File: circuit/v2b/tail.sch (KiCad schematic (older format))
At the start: 47 parts, among them J1 LED_DEBUG, J11 UART, J19 LiPo, J2 POWER_DEBUG, J25 USB_OTG, J3 LiPo, J9 DEBUG, Q1 Q_NMOS_GSD, SW1 SW_SPDT, U1 DWM1000, U2 EFM32HG222F64, U3 MC3630, U4 XC6215B332NR, U5 MCP73831-2-OT, Y1 32.768kHz CFPX-217 20ppm 7pF

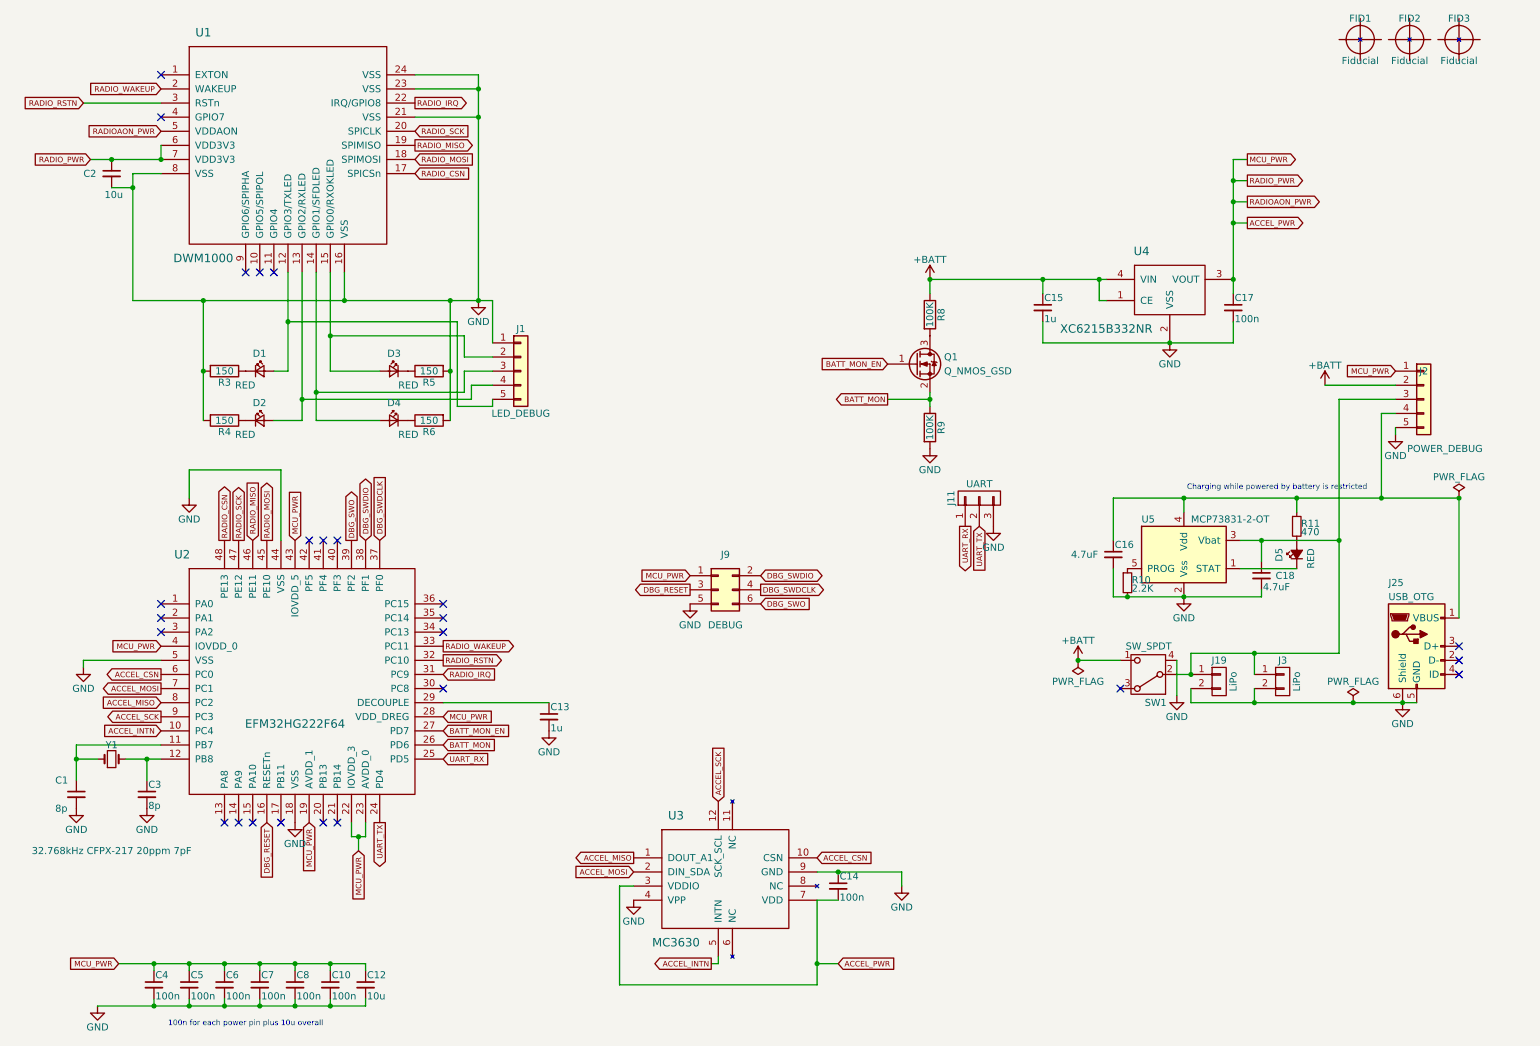
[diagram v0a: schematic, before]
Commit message: circuit: Add UART-USB level shifting and reduce charge current
We need to connect the UART to the USB data pins. As these will present
5 volts, we need to add level shifting to protect the 3.3 volt mcu.

We will need to enable the internal pullup on the UART Rx line.
The host cable we are proposing to use already has a pullup on its
Rx line.

While we're here, reduce the charge current to just under 200mA in
order to meet the 0.5C charge current specification on the 400mAh
batteries that we're using.

Signed-off-by: Gavan Fantom <gavan.fantom@unipart.io>
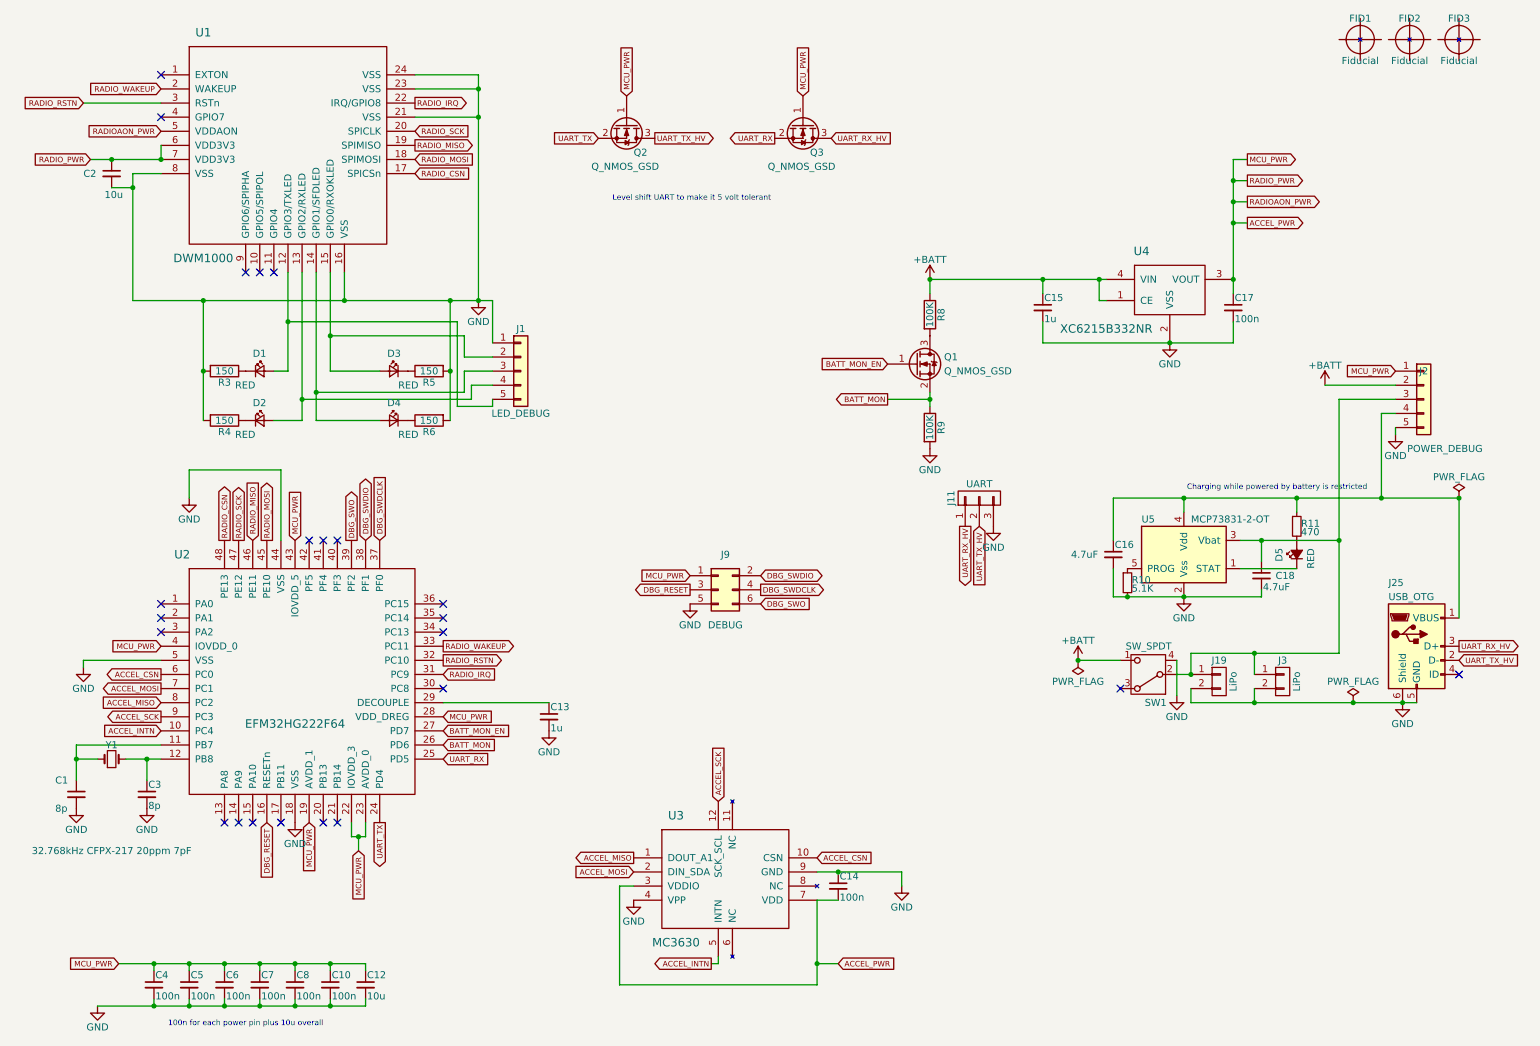
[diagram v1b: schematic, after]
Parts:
- added Q2, Q3: Q_NMOS_GSD, TO_SOT_Packages_SMD:SOT-323_SC-70, symbol Q_NMOS_GSD
- R10: value 2.2K -> 5.1K; MPN MCWR06X2201FTL -> MCWR06X5101FTL; SPN 2447320 -> 2447404
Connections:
- net ACCEL_PWR: now also Q2.1 (G), Q3.1 (G)
- net UART_RX: now also Q3.2 (S); no longer J11.1 (P1)
- net UART_TX: now also Q2.2 (S); no longer J11.2 (P2)
- net UART_TX_HV: now reaches J25.2 (D-)
- net UART_TX_HV: now also J11.2 (P2), Q2.3 (D)
- net UART_RX_HV: now reaches J25.3 (D+)
- net UART_RX_HV: now also J11.1 (P1), Q3.3 (D)
- no-connect marks 25 -> 23
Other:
- note added: "Level shift UART to make it 5 volt tolerant"
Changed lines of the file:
@@
 $EndComp
 $Comp
-L GND #PWR01
+L GND #PWR16
 U 1 1 58D90344
 P 8650 2850
-F 0 "#PWR01" H 8650 2600 50  0001 C CNN
+F 0 "#PWR16" H 8650 2600 50  0001 C CNN
 F 1 "GND" H 8650 2700 50  0000 C CNN
 F 2 "" H 8650 2850 50  0001 C CNN
@@
 $EndComp
 $Comp
-L +BATT #PWR02
+L +BATT #PWR12
 U 1 1 58D90443
 P 6950 2400
-F 0 "#PWR02" H 6950 2250 50  0001 C CNN
+F 0 "#PWR12" H 6950 2250 50  0001 C CNN
 F 1 "+BATT" H 6950 2540 50  0000 C CNN
 F 2 "" H 6950 2400 50  0001 C CNN
@@
 $EndComp
 $Comp
-L +BATT #PWR03
+L +BATT #PWR15
 U 1 1 58D91168
 P 8000 5100
-F 0 "#PWR03" H 8000 4950 50  0001 C CNN
+F 0 "#PWR15" H 8000 4950 50  0001 C CNN
 F 1 "+BATT" H 8000 5240 50  0000 C CNN
 F 2 "" H 8000 5100 50  0001 C CNN
@@
 $EndComp
 $Comp
-L GND #PWR04
+L GND #PWR11
 U 1 1 58E2BE94
 P 6750 6700
-F 0 "#PWR04" H 6750 6450 50  0001 C CNN
+F 0 "#PWR11" H 6750 6450 50  0001 C CNN
 F 1 "GND" H 6750 6550 50  0000 C CNN
 F 2 "" H 6750 6700 50  0001 C CNN
@@
 $EndComp
 $Comp
-L GND #PWR05
+L GND #PWR7
 U 1 1 58E32705
 P 3750 2550
-F 0 "#PWR05" H 3750 2300 50  0001 C CNN
+F 0 "#PWR7" H 3750 2300 50  0001 C CNN
 F 1 "GND" H 3750 2400 50  0000 C CNN
 F 2 "" H 3750 2550 50  0001 C CNN
@@
 $EndComp
 $Comp
-L GND #PWR06
+L GND #PWR13
 U 1 1 58E5097D
 P 6950 3600
-F 0 "#PWR06" H 6950 3350 50  0001 C CNN
+F 0 "#PWR13" H 6950 3350 50  0001 C CNN
 F 1 "GND" H 6950 3450 50  0000 C CNN
 F 2 "" H 6950 3600 50  0001 C CNN
@@
 P 8350 4550
 F 0 "R10" H 8380 4570 50  0000 L CNN
-F 1 "2.2K" H 8380 4510 50  0000 L CNN
+F 1 "5.1K" H 8380 4510 50  0000 L CNN
 F 2 "Resistors_SMD:R_0603" H 8350 4550 50  0001 C CNN
 F 3 "" H 8350 4550 50  0001 C CNN
 F 4 "Multicomp" H 0   0   50  0001 C CNN "MFR"
-F 5 "MCWR06X2201FTL" H 0   0   50  0001 C CNN "MPN"
-F 6 "Farnell" H 0   0   50  0001 C CNN "SPR"
-F 7 "2447320" H 0   0   50  0001 C CNN "SPN"
+F 5 "MCWR06X5101FTL" H 0   0   50  0001 C CNN "MPN"
+F 6 "Farnell" H 0   0   50  0001 C CNN "SPR"
+F 7 "2447404" H 0   0   50  0001 C CNN "SPN"
 F 8 "-" H 0   0   50  0001 C CNN "SPURL"
 	1    8350 4550
@@
 $EndComp
 $Comp
-L GND #PWR07
+L GND #PWR18
 U 1 1 58E581CA
 P 8750 4650
-F 0 "#PWR07" H 8750 4400 50  0001 C CNN
+F 0 "#PWR18" H 8750 4400 50  0001 C CNN
 F 1 "GND" H 8750 4500 50  0000 C CNN
 F 2 "" H 8750 4650 50  0001 C CNN
@@
 $EndComp
 $Comp
-L GND #PWR08
+L GND #PWR21
 U 1 1 58E5823C
 P 10300 5400
-F 0 "#PWR08" H 10300 5150 50  0001 C CNN
+F 0 "#PWR21" H 10300 5150 50  0001 C CNN
 F 1 "GND" H 10300 5250 50  0000 C CNN
 F 2 "" H 10300 5400 50  0001 C CNN
@@
 $EndComp
 $Comp
-L GND #PWR09
+L GND #PWR14
 U 1 1 58E62DAE
 P 7400 4150
-F 0 "#PWR09" H 7400 3900 50  0001 C CNN
+F 0 "#PWR14" H 7400 3900 50  0001 C CNN
 F 1 "GND" H 7400 4000 50  0000 C CNN
 F 2 "" H 7400 4150 50  0001 C CNN
@@
 $EndComp
 $Comp
-L GND #PWR010
+L GND #PWR10
 U 1 1 58ECBC0F
 P 5250 4700
-F 0 "#PWR010" H 5250 4450 50  0001 C CNN
+F 0 "#PWR10" H 5250 4450 50  0001 C CNN
 F 1 "GND" H 5250 4550 50  0000 C CNN
 F 2 "" H 5250 4700 50  0001 C CNN
@@
 $EndComp
 $Comp
-L GND #PWR011
+L GND #PWR6
 U 1 1 58ECC8B8
 P 2450 6250
-F 0 "#PWR011" H 2450 6000 50  0001 C CNN
+F 0 "#PWR6" H 2450 6000 50  0001 C CNN
 F 1 "GND" H 2450 6100 50  0000 C CNN
 F 2 "" H 2450 6250 50  0001 C CNN
@@
 $EndComp
 $Comp
-L GND #PWR012
+L GND #PWR2
 U 1 1 58ECC92E
 P 950 5150
-F 0 "#PWR012" H 950 4900 50  0001 C CNN
+F 0 "#PWR2" H 950 4900 50  0001 C CNN
 F 1 "GND" H 950 5000 50  0000 C CNN
 F 2 "" H 950 5150 50  0001 C CNN
@@
 $EndComp
 $Comp
-L GND #PWR013
+L GND #PWR5
 U 1 1 58ECCA91
 P 1700 3950
-F 0 "#PWR013" H 1700 3700 50  0001 C CNN
+F 0 "#PWR5" H 1700 3700 50  0001 C CNN
 F 1 "GND" H 1700 3800 50  0000 C CNN
 F 2 "" H 1700 3950 50  0001 C CNN
@@
 $EndComp
 $Comp
-L GND #PWR014
+L GND #PWR3
 U 1 1 58ECF8A7
 P 1050 7550
-F 0 "#PWR014" H 1050 7300 50  0001 C CNN
+F 0 "#PWR3" H 1050 7300 50  0001 C CNN
 F 1 "GND" H 1050 7400 50  0000 C CNN
 F 2 "" H 1050 7550 50  0001 C CNN
@@
 $EndComp
 $Comp
-L GND #PWR015
+L GND #PWR8
 U 1 1 58ED2393
 P 4250 5600
-F 0 "#PWR015" H 4250 5350 50  0001 C CNN
+F 0 "#PWR8" H 4250 5350 50  0001 C CNN
 F 1 "GND" H 4250 5450 50  0000 C CNN
 F 2 "" H 4250 5600 50  0001 C CNN
@@
 $EndComp
 $Comp
-L GND #PWR016
+L GND #PWR1
 U 1 1 58ED2E64
 P 900 6150
-F 0 "#PWR016" H 900 5900 50  0001 C CNN
+F 0 "#PWR1" H 900 5900 50  0001 C CNN
 F 1 "GND" H 900 6000 50  0000 C CNN
 F 2 "" H 900 6150 50  0001 C CNN
@@
 $EndComp
 $Comp
-L GND #PWR017
+L GND #PWR4
 U 1 1 58ED2EF0
 P 1400 6150
-F 0 "#PWR017" H 1400 5900 50  0001 C CNN
+F 0 "#PWR4" H 1400 5900 50  0001 C CNN
 F 1 "GND" H 1400 6000 50  0000 C CNN
 F 2 "" H 1400 6150 50  0001 C CNN
@@
 $EndComp
 $Comp
-L PWR_FLAG #FLG018
+L PWR_FLAG #FLG3
 U 1 1 58EFDE28
 P 10700 3950
-F 0 "#FLG018" H 10700 4025 50  0001 C CNN
+F 0 "#FLG3" H 10700 4025 50  0001 C CNN
 F 1 "PWR_FLAG" H 10700 4100 50  0000 C CNN
 F 2 "" H 10700 3950 50  0001 C CNN
@@
 $EndComp
 $Comp
-L PWR_FLAG #FLG019
+L PWR_FLAG #FLG2
 U 1 1 58F0C76B
 P 9950 5400
-F 0 "#FLG019" H 9950 5475 50  0001 C CNN
+F 0 "#FLG2" H 9950 5475 50  0001 C CNN
 F 1 "PWR_FLAG" H 9950 5550 50  0000 C CNN
 F 2 "" H 9950 5400 50  0001 C CNN
@@
 $EndComp
 $Comp
-L GND #PWR020
+L GND #PWR9
 U 1 1 590A2FEB
 P 4850 6800
-F 0 "#PWR020" H 4850 6550 50  0001 C CNN
+F 0 "#PWR9" H 4850 6550 50  0001 C CNN
 F 1 "GND" H 4850 6650 50  0000 C CNN
 F 2 "" H 4850 6800 50  0001 C CNN
@@
 Charging while powered by battery is restricted
 Text GLabel 7300 4150 3    39   Input ~ 0
-UART_TX
+UART_TX_HV
 Text GLabel 7200 4150 3    39   Output ~ 0
-UART_RX
+UART_RX_HV
 Text GLabel 3050 6250 3    39   Output ~ 0
 UART_TX
@@
 Connection ~ 9100 2000
 Connection ~ 6950 2400
-NoConn ~ 10700 5000
-NoConn ~ 10700 5100
 NoConn ~ 10700 5200
 NoConn ~ 2750 6250
@@
 NoConn ~ 8300 5300
 $Comp
-L PWR_FLAG #FLG021
+L PWR_FLAG #FLG1
 U 1 1 5BB39745
 P 8000 5100
-F 0 "#FLG021" H 8000 5175 50  0001 C CNN
+F 0 "#FLG1" H 8000 5175 50  0001 C CNN
 F 1 "PWR_FLAG" H 8000 5250 50  0000 C CNN
 F 2 "" H 8000 5100 50  0001 C CNN
@@
 Connection ~ 8000 5100
 $Comp
-L GND #PWR022
+L GND #PWR17
 U 1 1 5BB3B459
 P 8700 5350
-F 0 "#PWR022" H 8700 5100 50  0001 C CNN
+F 0 "#PWR17" H 8700 5100 50  0001 C CNN
 F 1 "GND" H 8700 5200 50  0000 C CNN
 F 2 "" H 8700 5350 50  0001 C CNN
@@
 $EndComp
 $Comp
-L GND #PWR023
+L GND #PWR20
 U 1 1 5C40F853
 P 10250 3500
-F 0 "#PWR023" H 10250 3250 50  0001 C CNN
+F 0 "#PWR20" H 10250 3250 50  0001 C CNN
 F 1 "GND" H 10250 3350 50  0000 C CNN
 F 2 "" H 10250 3500 50  0001 C CNN
@@
 Connection ~ 9850 4250
 $Comp
-L +BATT #PWR024
+L +BATT #PWR19
 U 1 1 5C4110FB
 P 9750 3150
-F 0 "#PWR024" H 9750 3000 50  0001 C CNN
+F 0 "#PWR19" H 9750 3000 50  0001 C CNN
 F 1 "+BATT" H 9750 3290 50  0000 C CNN
 F 2 "" H 9750 3150 50  0001 C CNN
@@
 	9250 5300 9250 5400
 Connection ~ 9250 5400
+$Comp
+L Q_NMOS_GSD Q2
+U 1 1 5CCC2EF8
+P 4800 1300
+F 0 "Q2" V 5000 1350 50  0000 L CNN
+F 1 "Q_NMOS_GSD" V 5100 1050 50  0000 L CNN
+F 2 "TO_SOT_Packages_SMD:SOT-323_SC-70" H 5000 1400 50  0001 C CNN
+F 3 "" H 4800 1300 50  0001 C CNN
+F 4 "Nexperia" H -2050 -1700 50  0001 C CNN "MFR"
+F 5 "NX3020NAKW" H -2050 -1700 50  0001 C CNN "MPN"
+F 6 "Farnell" H -2050 -1700 50  0001 C CNN "SPR"
+F 7 "2311183" H -2050 -1700 50  0001 C CNN "SPN"
+F 8 "-" H -2050 -1700 50  0001 C CNN "SPURL"
+	1    4800 1300
+	0    1    1    0
+$EndComp
+$Comp
+L Q_NMOS_GSD Q3
+U 1 1 5CCC32FE
+P 6050 1300
+F 0 "Q3" V 6250 1350 50  0000 L CNN
+F 1 "Q_NMOS_GSD" V 6350 1050 50  0000 L CNN
+F 2 "TO_SOT_Packages_SMD:SOT-323_SC-70" H 6250 1400 50  0001 C CNN
+F 3 "" H 6050 1300 50  0001 C CNN
+F 4 "Nexperia" H -800 -1700 50  0001 C CNN "MFR"
+F 5 "NX3020NAKW" H -800 -1700 50  0001 C CNN "MPN"
+F 6 "Farnell" H -800 -1700 50  0001 C CNN "SPR"
+F 7 "2311183" H -800 -1700 50  0001 C CNN "SPN"
+F 8 "-" H -800 -1700 50  0001 C CNN "SPURL"
+	1    6050 1300
+	0    1    1    0
+$EndComp
+Text GLabel 4600 1400 0    39   Input ~ 0
+UART_TX
+Text GLabel 5000 1400 2    39   Output ~ 0
+UART_TX_HV
+Text GLabel 5850 1400 0    39   Output ~ 0
+UART_RX
+Text GLabel 6250 1400 2    39   Input ~ 0
+UART_RX_HV
+Text GLabel 4800 1100 1    39   Input ~ 0
+MCU_PWR
+Text GLabel 6050 1100 1    39   Input ~ 0
+MCU_PWR
+Text GLabel 10700 5100 2    39   Input ~ 0
+UART_TX_HV
+Text GLabel 10700 5000 2    39   Output ~ 0
+UART_RX_HV
+Text Notes 4700 1850 0    39   ~ 0
+Level shift UART to make it 5 volt tolerant
 $EndSCHEMATC
